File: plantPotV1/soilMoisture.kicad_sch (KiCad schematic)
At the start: 1 part, among them J1 Conn_01x03_Socket

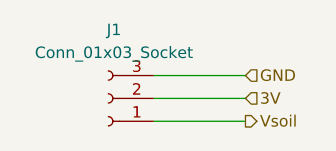
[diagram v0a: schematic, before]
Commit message: updated circuit diagram (top only)
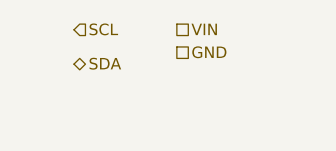
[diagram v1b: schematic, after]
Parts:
- removed J1: Conn_01x03_Socket, symbol Connector:Conn_01x03_Socket
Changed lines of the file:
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@@
 		(comment 4 "Stanford University")
 	)
-	(wire
-		(pts
-			(xy 60.96 80.01) (xy 71.12 80.01)
-		)
-		(stroke
-			(width 0)
-			(type default)
-		)
-	)
-	(wire
-		(pts
-			(xy 60.96 82.55) (xy 71.12 82.55)
-		)
-		(stroke
-			(width 0)
-			(type default)
-		)
-	)
-	(wire
-		(pts
-			(xy 60.96 85.09) (xy 71.12 85.09)
-		)
-		(stroke
-			(width 0)
-			(type default)
-		)
-	)
-	(hierarchical_label "Vsoil"
-		(shape output)
-		(at 71.12 85.09 0)
+	(hierarchical_label "SDA"
+		(shape bidirectional)
+		(at 52.07 78.74 0)
 		(fields_autoplaced yes)
 		(effects
@@
 		)
 	)
-	(hierarchical_label "3V"
+	(hierarchical_label "SCL"
 		(shape input)
-		(at 71.12 82.55 0)
+		(at 52.07 74.93 0)
+		(fields_autoplaced yes)
+		(effects
+			(font
+				(size 1.27 1.27)
+			)
+			(justify left)
+		)
+	)
+	(hierarchical_label "VIN"
+		(shape passive)
+		(at 63.5 74.93 0)
 		(fields_autoplaced yes)
 		(effects
@@
 	)
 	(hierarchical_label "GND"
-		(shape input)
-		(at 71.12 80.01 0)
+		(shape passive)
+		(at 63.5 77.47 0)
 		(fields_autoplaced yes)
 		(effects
@@
 		)
 	)
-	(symbol
-		(lib_id "Connector:Conn_01x03_Socket")
-		(at 55.88 82.55 180)
-		(unit 1)
-		(exclude_from_sim no)
-		(in_bom yes)
-		(on_board yes)
-		(dnp no)
-		(fields_autoplaced yes)
-		(property "Reference" "J1"
-			(at 56.515 74.93 0)
-			(effects
-				(font
-					(size 1.27 1.27)
-				)
-			)
-		)
-		(property "Value" "Conn_01x03_Socket"
-			(at 56.515 77.47 0)
-			(effects
-				(font
-					(size 1.27 1.27)
-				)
-			)
-		)
-		(property "Footprint" ""
-			(at 55.88 82.55 0)
-			(effects
-				(font
-					(size 1.27 1.27)
-				)
-				(hide yes)
-			)
-		)
-		(property "Datasheet" "~"
-			(at 55.88 82.55 0)
-			(effects
-				(font
-					(size 1.27 1.27)
-				)
-				(hide yes)
-			)
-		)
-		(property "Description" "Generic connector, single row, 01x03, script generated"
-			(at 55.88 82.55 0)
-			(effects
-				(font
-					(size 1.27 1.27)
-				)
-				(hide yes)
-			)
-		)
-		(pin "1"
-		)
-		(pin "2"
-		)
-		(pin "3"
-		)
-		(instances
-			(project ""
-				(path "/bd24c4db-4e36-4117-bd4f-5228ef241da9/81557b54-15f5-4940-a529-3d8baf627000"
-					(reference "J1")
-					(unit 1)
-				)
-			)
-		)
-	)
